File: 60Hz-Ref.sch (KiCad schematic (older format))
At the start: 8 parts

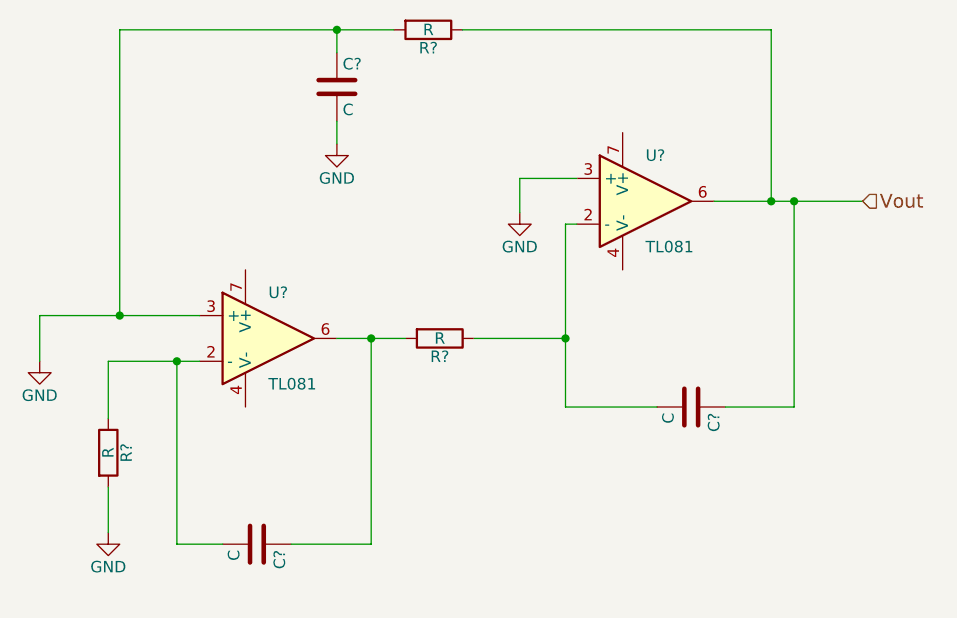
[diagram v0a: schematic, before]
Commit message: Added the basic Schematic
PWM generators work for given reference design values. (LAB Tested)
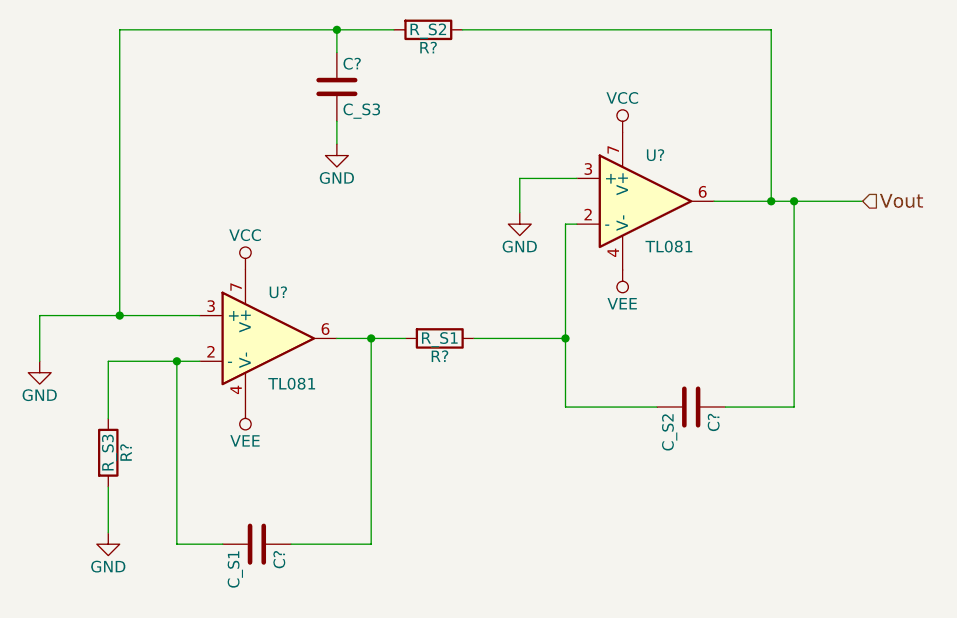
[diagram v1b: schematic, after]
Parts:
- C?: value C -> C_S2
- C?: value C -> C_S1
- C?: value C -> C_S3
- R?: value R -> R_S1
- R?: value R -> R_S3
- R?: value R -> R_S2
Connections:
- net VEE: now reaches U?.4 (V-)
- net VEE: now also U?.4 (V-)
- net VCC: now reaches U?.7 (V+)
- net VCC: now also U?.7 (V+)
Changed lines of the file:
@@
 LIBS:contrib
 LIBS:valves
-LIBS:Buck Supply-cache
 LIBS:H-Bridge PWM Switching Circuit-cache
 EELAYER 25 0
@@
 P 3950 4200
 F 0 "R?" V 4030 4200 50  0000 C CNN
-F 1 "R" V 3950 4200 50  0000 C CNN
+F 1 "R_S1" V 3950 4200 50  0000 C CNN
 F 2 "" V 3880 4200 50  0000 C CNN
 F 3 "" H 3950 4200 50  0000 C CNN
@@
 P 5050 4500
 F 0 "C?" H 5075 4600 50  0000 L CNN
-F 1 "C" H 5075 4400 50  0000 L CNN
+F 1 "C_S2" H 5075 4400 50  0000 L CNN
 F 2 "" H 5088 4350 50  0000 C CNN
 F 3 "" H 5050 4500 50  0000 C CNN
@@
 P 2500 4700
 F 0 "R?" V 2580 4700 50  0000 C CNN
-F 1 "R" V 2500 4700 50  0000 C CNN
+F 1 "R_S3" V 2500 4700 50  0000 C CNN
 F 2 "" V 2430 4700 50  0000 C CNN
 F 3 "" H 2500 4700 50  0000 C CNN
@@
 P 3150 5100
 F 0 "C?" H 3175 5200 50  0000 L CNN
-F 1 "C" H 3175 5000 50  0000 L CNN
+F 1 "C_S1" H 3175 5000 50  0000 L CNN
 F 2 "" H 3188 4950 50  0000 C CNN
 F 3 "" H 3150 5100 50  0000 C CNN
@@
 P 3500 3100
 F 0 "C?" H 3525 3200 50  0000 L CNN
-F 1 "C" H 3525 3000 50  0000 L CNN
+F 1 "C_S3" H 3525 3000 50  0000 L CNN
 F 2 "" H 3538 2950 50  0000 C CNN
 F 3 "" H 3500 3100 50  0000 C CNN
@@
 P 3900 2850
 F 0 "R?" V 3980 2850 50  0000 C CNN
-F 1 "R" V 3900 2850 50  0000 C CNN
+F 1 "R_S2" V 3900 2850 50  0000 C CNN
 F 2 "" V 3830 2850 50  0000 C CNN
 F 3 "" H 3900 2850 50  0000 C CNN
@@
 Wire Wire Line
 	3500 3250 3500 3350
+$Comp
+L VCC #PWR?
+U 1 1 58EFDF12
+P 3100 3900
+F 0 "#PWR?" H 3100 3750 50  0001 C CNN
+F 1 "VCC" H 3100 4050 50  0000 C CNN
+F 2 "" H 3100 3900 50  0000 C CNN
+F 3 "" H 3100 3900 50  0000 C CNN
+	1    3100 3900
+	1    0    0    -1
+$EndComp
+$Comp
+L VCC #PWR?
+U 1 1 58EFDF3E
+P 4750 3300
+F 0 "#PWR?" H 4750 3150 50  0001 C CNN
+F 1 "VCC" H 4750 3450 50  0000 C CNN
+F 2 "" H 4750 3300 50  0000 C CNN
+F 3 "" H 4750 3300 50  0000 C CNN
+	1    4750 3300
+	1    0    0    -1
+$EndComp
+$Comp
+L VEE #PWR?
+U 1 1 58EFDF6A
+P 4750 3900
+F 0 "#PWR?" H 4750 3750 50  0001 C CNN
+F 1 "VEE" H 4750 4050 50  0000 C CNN
+F 2 "" H 4750 3900 50  0000 C CNN
+F 3 "" H 4750 3900 50  0000 C CNN
+	1    4750 3900
+	-1   0    0    1
+$EndComp
+$Comp
+L VEE #PWR?
+U 1 1 58EFDF96
+P 3100 4500
+F 0 "#PWR?" H 3100 4350 50  0001 C CNN
+F 1 "VEE" H 3100 4650 50  0000 C CNN
+F 2 "" H 3100 4500 50  0000 C CNN
+F 3 "" H 3100 4500 50  0000 C CNN
+	1    3100 4500
+	-1   0    0    1
+$EndComp
 $EndSCHEMATC
